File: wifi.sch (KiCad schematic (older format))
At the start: 1 part

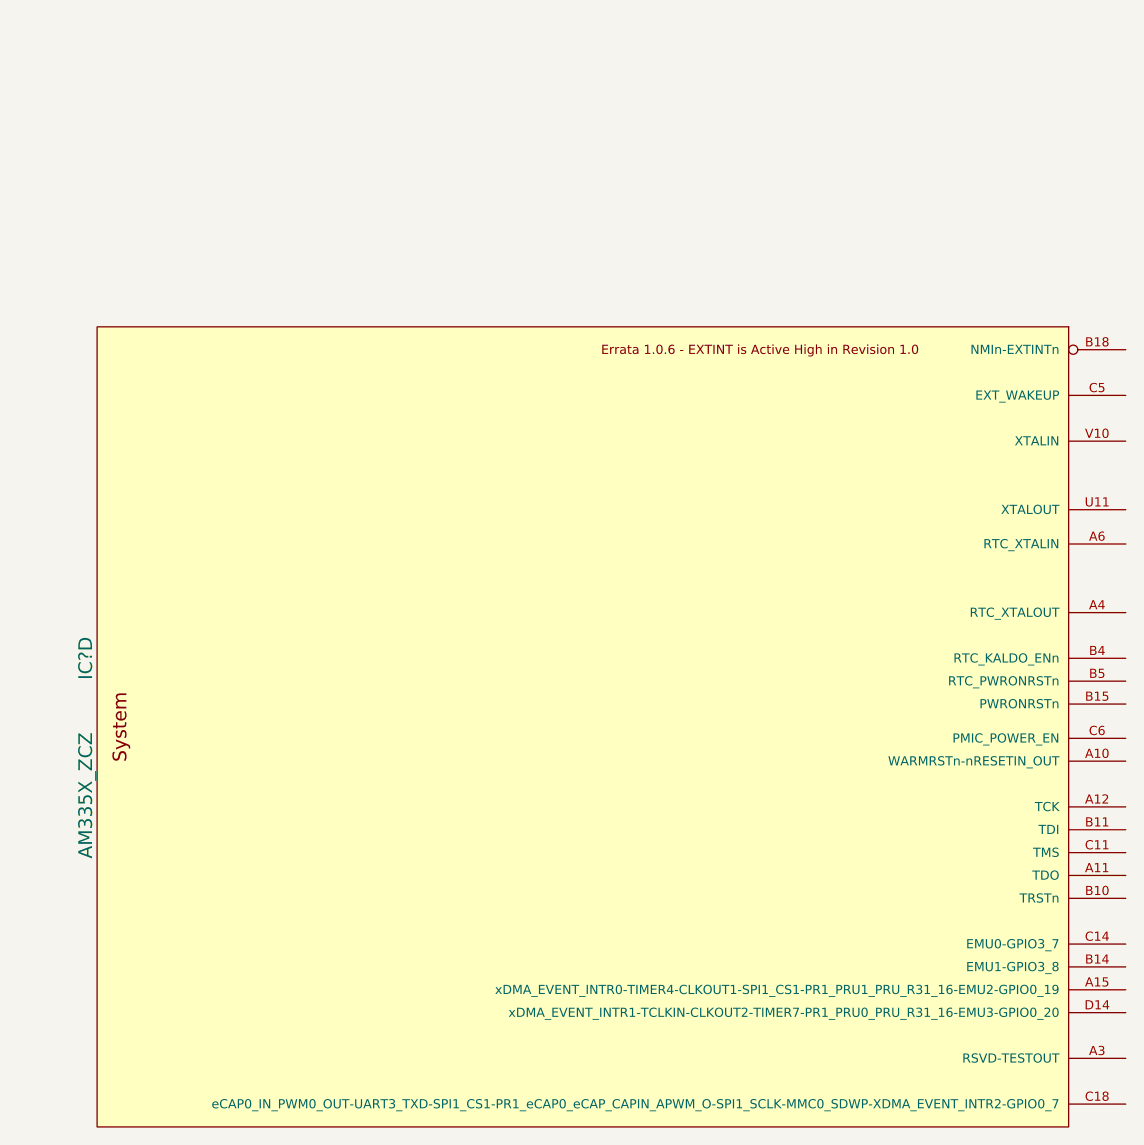
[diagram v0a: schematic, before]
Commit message: hierarchical sheets defined
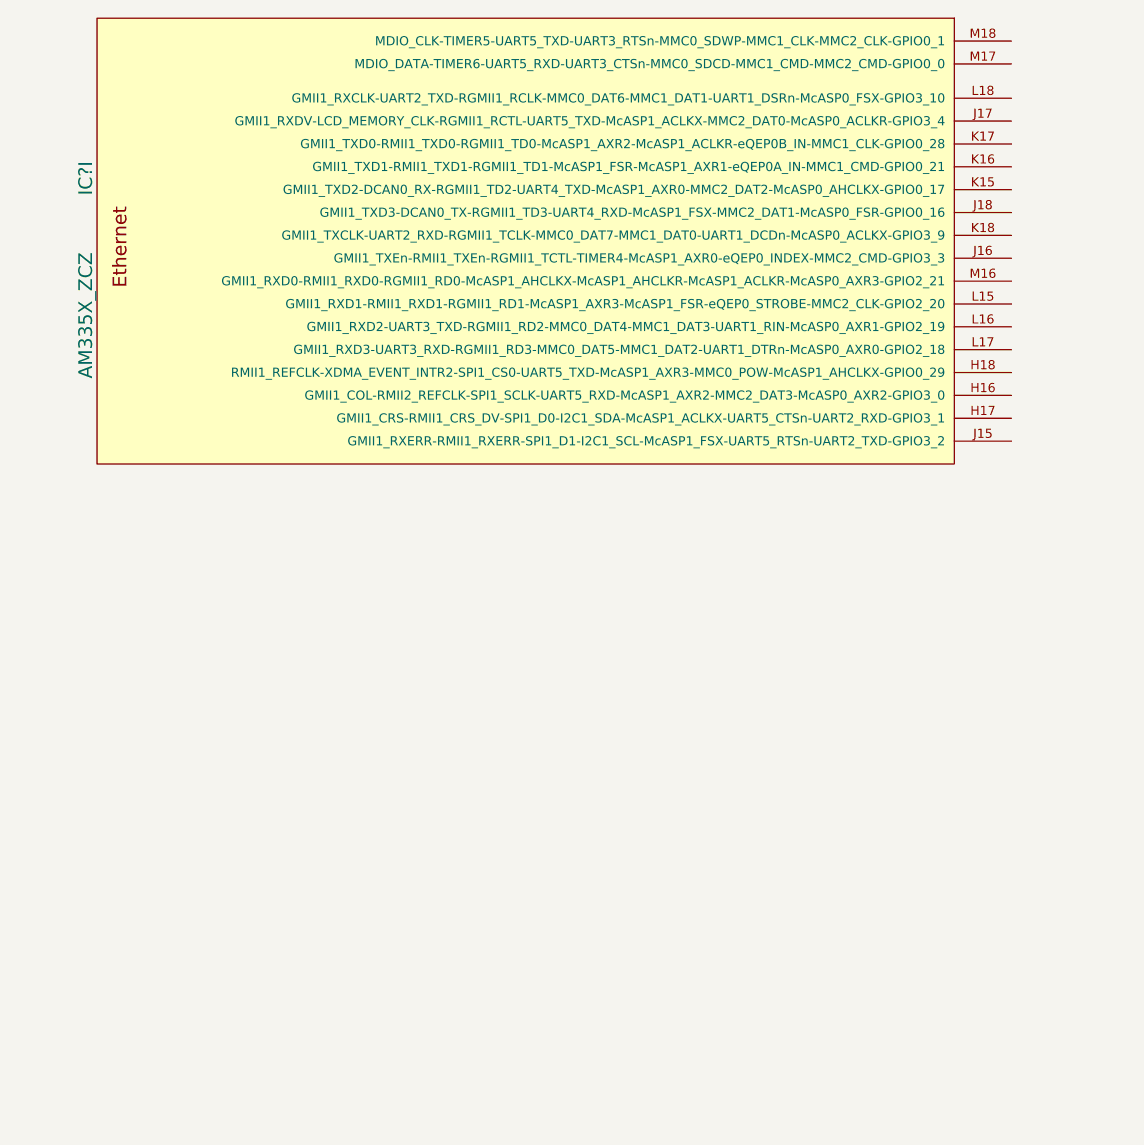
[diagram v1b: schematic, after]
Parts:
- removed IC?: AM335X_ZCZ, symbol AM335X_ZCZ
- added IC?: AM335X_ZCZ, symbol AM335X_ZCZ
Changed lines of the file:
@@
 $Descr A4 11693 8268
 encoding utf-8
-Sheet 6 9
+Sheet 9 9
 Title ""
 Date ""
@@
 $Comp
 L AM335X_ZCZ IC?
-U 4 1 58AC1D57
-P 725 3800
-AR Path="/58AC1D57" Ref="IC?"  Part="4"
-AR Path="/58AC1B74/58AC1D57" Ref="IC?"  Part="4"
-F 0 "IC?" V 675 4100 60  0000 C CNN
-F 1 "AM335X_ZCZ" V 675 3500 60  0000 C CNN
-F 2 "" H 725 3800 60  0001 C CNN
-F 3 "" H 725 3800 60  0001 C CNN
-	4    725  3800
+U 9 1 58AD666B
+P 725 1700
+F 0 "IC?" V 675 2000 60  0000 C CNN
+F 1 "AM335X_ZCZ" V 675 1400 60  0000 C CNN
+F 2 "" H 725 1700 60  0001 C CNN
+F 3 "" H 725 1700 60  0001 C CNN
+	9    725  1700
 	1    0    0    -1
 $EndComp

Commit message: wip wifi
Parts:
- added C? (x2): 100nF/6.3V, symbol C
- added R? (x7): 33, symbol R
- added R?: 1.5k, symbol R
- added R? (x6): 10k, symbol R
- added U?: TXS0108, symbol TXB0108
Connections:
- net WL_SDIO_D3.CPU: now reaches IC?.H16 (GMII1_COL-RMII2_REFCLK-SPI1_SCLK-UART5_RXD-McASP1_AXR2-MMC2_DAT3-McASP0_AXR2-GPIO3_0)
- net WL_SDIO_D3.CPU: now also R?.1
- net WL_IRQ.CPU: now reaches IC?.H18 (RMII1_REFCLK-XDMA_EVENT_INTR2-SPI1_CS0-UART5_TXD-McASP1_AXR3-MMC0_POW-McASP1_AHCLKX-GPIO0_29)
- net WL_SDIO_CMD.CPU: now reaches IC?.J16 (GMII1_TXEn-RMII1_TXEn-RGMII1_TCTL-TIMER4-McASP1_AXR0-eQEP0_INDEX-MMC2_CMD-GPIO3_3)
- net WL_SDIO_CMD.CPU: now also R?.1
- net WL_SDIO_D0.CPU: now reaches IC?.J17 (GMII1_RXDV-LCD_MEMORY_CLK-RGMII1_RCTL-UART5_TXD-McASP1_ACLKX-MMC2_DAT0-McASP0_ACLKR-GPIO3_4)
- net WL_SDIO_D0.CPU: now also R?.1
- net WL_SDIO_D1.CPU: now reaches IC?.J18 (GMII1_TXD3-DCAN0_TX-RGMII1_TD3-UART4_RXD-McASP1_FSX-MMC2_DAT1-McASP0_FSR-GPIO0_16)
- net WL_SDIO_D1.CPU: now also R?.1
- net WL_SDIO_D2.CPU: now reaches IC?.K15 (GMII1_TXD2-DCAN0_RX-RGMII1_TD2-UART4_TXD-McASP1_AXR0-MMC2_DAT2-McASP0_AHCLKX-GPIO0_17)
- net WL_SDIO_D2.CPU: now also R?.1
- net BT_EN.CPU: now reaches IC?.K17 (GMII1_TXD0-RMII1_TXD0-RGMII1_TD0-McASP1_AXR2-McASP1_ACLKR-eQEP0B_IN-MMC1_CLK-GPIO0_28)
- net WL_EN.CPU: now reaches IC?.K18 (GMII1_TXCLK-UART2_RXD-RGMII1_TCLK-MMC0_DAT7-MMC1_DAT0-UART1_DCDn-McASP0_ACLKX-GPIO3_9)
- net WL_SDIO_CLK.CPU: now reaches IC?.L15 (GMII1_RXD1-RMII1_RXD1-RGMII1_RD1-McASP1_AXR3-McASP1_FSR-eQEP0_STROBE-MMC2_CLK-GPIO2_20)
- net WL_SDIO_CLK.CPU: now also R?.1
- net BT_HCI_TX.CPU: now reaches IC?.L16 (GMII1_RXD2-UART3_TXD-RGMII1_RD2-MMC0_DAT4-MMC1_DAT3-UART1_RIN-McASP0_AXR1-GPIO2_19)
- net BT_HCI_RX.CPU: now reaches IC?.L17 (GMII1_RXD3-UART3_RXD-RGMII1_RD3-MMC0_DAT5-MMC1_DAT2-UART1_DTRn-McASP0_AXR0-GPIO2_18)
- net LS_BUF_OE.CPU: now reaches IC?.L18 (GMII1_RXCLK-UART2_TXD-RGMII1_RCLK-MMC0_DAT6-MMC1_DAT1-UART1_DSRn-McASP0_FSX-GPIO3_10)
- net LS_BUF_OE.CPU: now also R?.2
- net BT_HCI_CTS.CPU: now reaches IC?.M17 (MDIO_DATA-TIMER6-UART5_RXD-UART3_CTSn-MMC0_SDCD-MMC1_CMD-MMC2_CMD-GPIO0_0)
- net BT_HCI_RTS.CPU: now reaches IC?.M18 (MDIO_CLK-TIMER5-UART5_TXD-UART3_RTSn-MMC0_SDWP-MMC1_CLK-MMC2_CLK-GPIO0_1)
- new net: R?.2, U?.14 (B6)
- new net: R?.2, U?.15 (B5)
- new net: R?.2, U?.16 (B4)
- new net: R?.2, U?.17 (B3)
- new net: R?.2, U?.18 (B2)
- new net: R?.2, U?.20 (B1)
- new net GNDD: C?.1, C?.1, R?.1, U?.11 (GND)
- new net LS_BUF_OE: R?.1, R?.2, U?.10 (^OE)
- new net VDD_1V8_WIFI: C?.2, R?.1, R?.1, R?.1, R?.1, R?.1, R?.1, U?.2 (VccA)
- new net VDD_3V3_WIFI: C?.2, U?.19 (VccB)
- new net WL_SDIO_CLK: R?.2, U?.6 (A5)
- new net WL_SDIO_CMD: R?.2, U?.7 (A6)
- new net WL_SDIO_D0: R?.2, U?.1 (A1)
- new net WL_SDIO_D1: R?.2, U?.3 (A2)
- new net WL_SDIO_D2: R?.2, U?.4 (A3)
- new net WL_SDIO_D3: R?.2, U?.5 (A4)
- no-connect marks 0 -> 8

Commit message: wip wl1835 lib
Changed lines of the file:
@@
 EESchema Schematic File Version 2
+LIBS:mateboard-rescue
 LIBS:power
 LIBS:device
@@
 $EndComp
 Wire Wire Line
-	2950 3825 2950 3875
-Wire Wire Line
-	2950 3875 2950 3925
+	2950 3825 2950 3925
 Wire Wire Line
 	2950 3925 3000 3925
@@
 $EndComp
 Wire Wire Line
-	4300 3825 4300 3875
-Wire Wire Line
-	4300 3875 4300 3925
+	4300 3825 4300 3925
 Wire Wire Line
 	4300 3925 4200 3925
@@
 	1200 4825 2025 4825
 Wire Wire Line
-	2325 4825 2425 4825
-Wire Wire Line
-	2425 4825 3000 4825
+	2325 4825 3000 4825
 Wire Wire Line
 	2425 4875 2425 4825
@@
 	1100 4525 3000 4525
 Wire Wire Line
-	1100 3425 1100 3475
-Wire Wire Line
-	1100 3475 1100 3625
-Wire Wire Line
-	1100 3475 1225 3475
-Wire Wire Line
-	1225 3475 1350 3475
-Wire Wire Line
-	1350 3475 1475 3475
-Wire Wire Line
-	1475 3475 1600 3475
-Wire Wire Line
-	1600 3475 1725 3475
+	1100 3425 1100 3625
+Wire Wire Line
+	1100 3475 1725 3475
 Wire Wire Line
 	1725 3475 1725 3625

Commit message: wifi bt done
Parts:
- added AE?: ACA-5036-A2-CC-S, symbol Antenna_Shield
- added C? (x4): 100nF/6.3V, symbol C
- added C? (x3): 10pF, symbol C
- added C?: 1uF/6.3V, symbol C
- added C?: DNP 47uF, symbol CP
- added C?: 10uF/6.3V, symbol C
- added IC?: WL1835MODGBMOCT, symbol WL1835MODGBMOCT
- added J? (x2): ANT2, symbol CONN_COAXIAL
- added J? (x9): TEST_1P, symbol TEST_1P
- added R? (x14): 33, symbol R
- added R? (x2): 150k, symbol R
- added R? (x2): DNP 1k, symbol R
- added R?: DNP 10k, symbol R
- added R?: 1k, symbol R
- added R?: DNP 0R, symbol R
- added U?: TXS0108, symbol TXB0108
- added X?: NZ2520SB-32.768KHZ-NSA3534C, symbol OSCILLATOR
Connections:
- net BT_EN.CPU: now also R?.2
- net BT_HCI_CTS.CPU: now also R?.2, U?.15 (B5)
- net BT_HCI_RTS.CPU: now also R?.2, U?.13 (B7)
- net BT_HCI_RX.CPU: now also U?.14 (B6)
- net BT_HCI_TX.CPU: now also U?.20 (B1)
- net GNDD: now also AE?.2 (Shield), C?.1, C?.1, C?.1, C?.2, C?.2, C?.2, C?.2, IC?.1 (GND), IC?.15 (GND), IC?.16 (GND), IC?.17 (GND), IC?.19 (GND), IC?.20 (GND), IC?.23 (GND), IC?.24 (GND), IC?.28 (GND), IC?.29 (GND), IC?.30 (GND), IC?.31 (GND), IC?.33 (GND), IC?.34 (GND), IC?.35 (GND), IC?.37 (GND), IC?.39 (GND), IC?.44 (GND), IC?.45 (GND), IC?.48 (GND), IC?.49 (GND), IC?.54 (GND), IC?.55 (GND), IC?.59 (GND), IC?.61 (GND), IC?.63 (GND), IC?.64 (GND), IC?.7 (GND), IC?.9 (GND), IC?.PAD (G1-G36), J?.2 (Ext), J?.2 (Ext), R?.1, R?.1, R?.1, R?.1, U?.11 (GND), X?.2 (GND)
- net LS_BUF_OE: now also U?.10 (^OE)
- net VDD_1V8_WIFI: now also C?.1, C?.1, C?.2, C?.2, IC?.38 (VIO), R?.1, R?.1, U?.2 (VccA), X?.4 (VDD)
- net VDD_3V3_WIFI: now also C?.1, C?.1, C?.2, IC?.46 (VBAT_IN), IC?.47 (VBAT_IN), U?.19 (VccB)
- net WL_EN.CPU: now also R?.2
- net WL_IRQ.CPU: now also R?.2
- net WL_SDIO_CLK: now also R?.2
- net WL_SDIO_CMD: now also R?.2
- net WL_SDIO_D0: now also R?.2
- net WL_SDIO_D1: now also R?.2
- net WL_SDIO_D2: now also R?.2
- net WL_SDIO_D3: now also R?.2
- new net: IC?.10 (WL_SDIO_D0), R?.1
- new net: IC?.11 (WL_SDIO_D1), R?.1
- new net: IC?.12 (WL_SDIO_D2), R?.1
- new net: IC?.13 (WL_SDIO_D3), R?.1
- new net: IC?.14 (WLAN_IRQ), R?.1, R?.2
- new net: C?.1, IC?.18 (RF_ANT2)
- new net: IC?.25 (GPIO4), J?.1
- new net: IC?.26 (GPIO2), J?.1
- new net: IC?.27 (GPIO1), J?.1
- new net: C?.1, C?.2, IC?.32 (RF_ANT1)
- new net: IC?.42 (WL_UART_DBG), J?.1
- new net: IC?.43 (BT_UART_DBG), J?.1
- new net: IC?.50 (BT_HCI_RTS), R?.2
- new net: IC?.51 (BT_HCI_CTS), R?.2
- new net: IC?.52 (BT_HCI_TX), R?.2
- new net: IC?.53 (BT_HCI_RX), R?.2
- new net: IC?.56 (BT_AUD_IN), J?.1
- new net: IC?.57 (BT_AUD_OUT), J?.1
- new net: IC?.58 (BT_AUD_FSYNC), J?.1
- new net: IC?.6 (WL_SDIO_CMD), R?.1
- new net: IC?.60 (BT_AUD_CLK), J?.1
- new net: IC?.8 (WL_SDIO_CLK), R?.1
- new net: R?.1, U?.12 (B8)
- new net: R?.1, U?.17 (B3)
- new net: R?.1, U?.18 (B2)
- new net: C?.2, J?.1 (In) (x2)
- new net: AE?.1 (A), C?.1
- new net: R?.2, X?.1 (EN)
- new net 32.768kHz: IC?.36 (EXT_32K), R?.2, X?.3 (OUT)
- new net BT_EN: IC?.41 (BT_EN), R?.2, U?.4 (A3)
- new net BT_HCI_CTS: R?.1, U?.8 (A7)
- new net BT_HCI_RTS: R?.1, U?.6 (A5)
- new net BT_HCI_RX: R?.1, U?.1 (A1)
- new net BT_HCI_TX: R?.1, U?.7 (A6)
- new net CLKOUT2: U?.16 (B4)
- new net SLOW_CLK: R?.1, U?.5 (A4)
- new net WL_EN: IC?.40 (WLAN_EN), R?.2, U?.3 (A2)
- new net WL_IRQ: R?.2, U?.9 (A8)
- no-connect marks 8 -> 12
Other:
- note added: "Required to put\ndevice in debug\nmode."

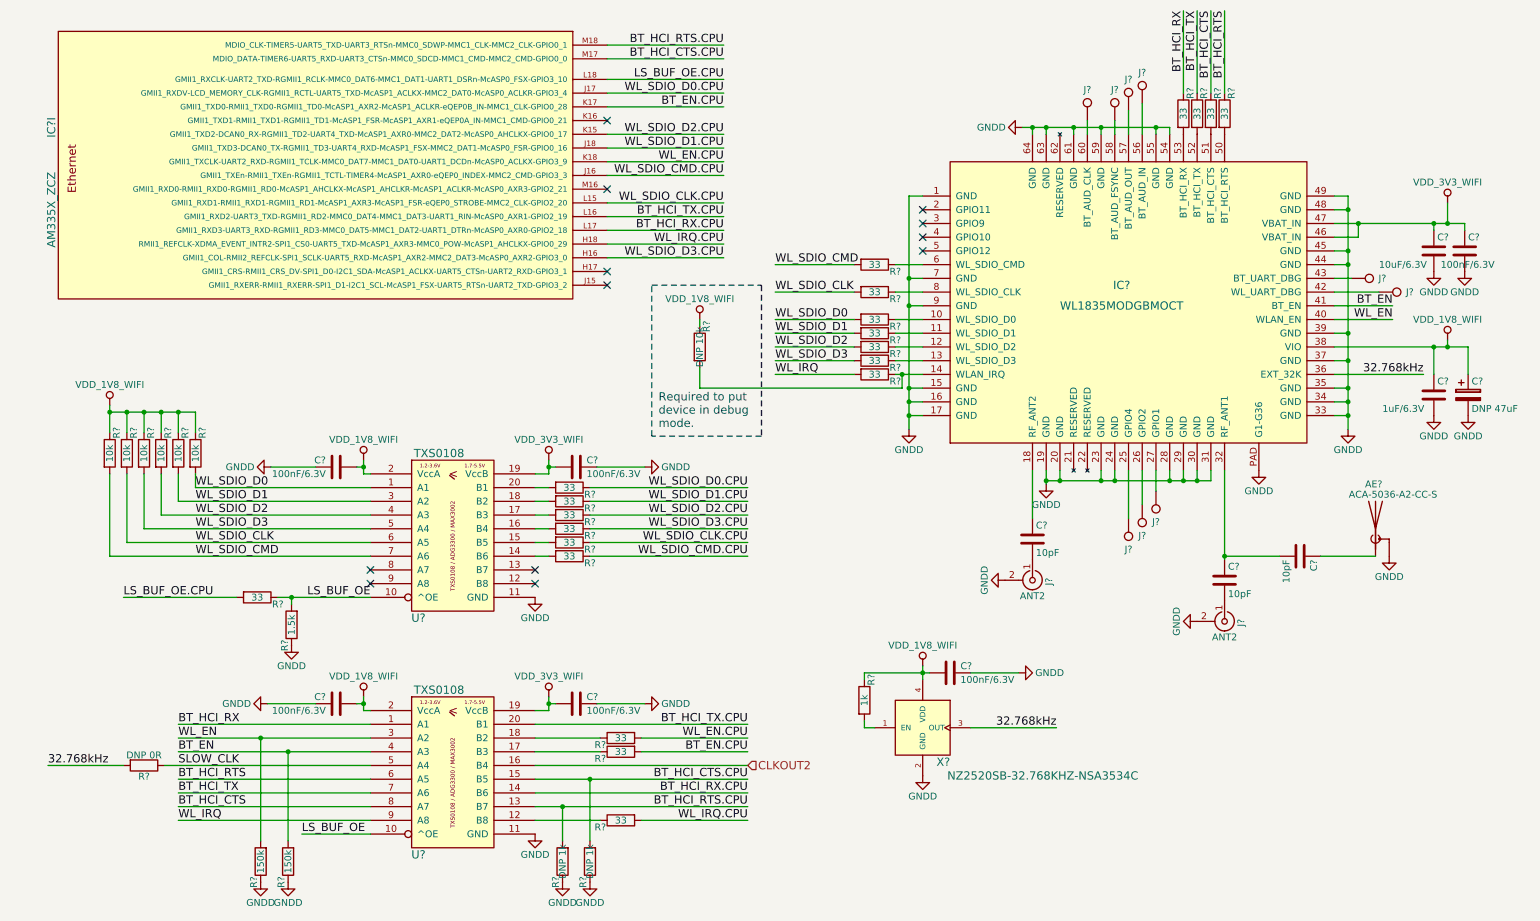
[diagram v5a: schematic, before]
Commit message: wifi bt leds
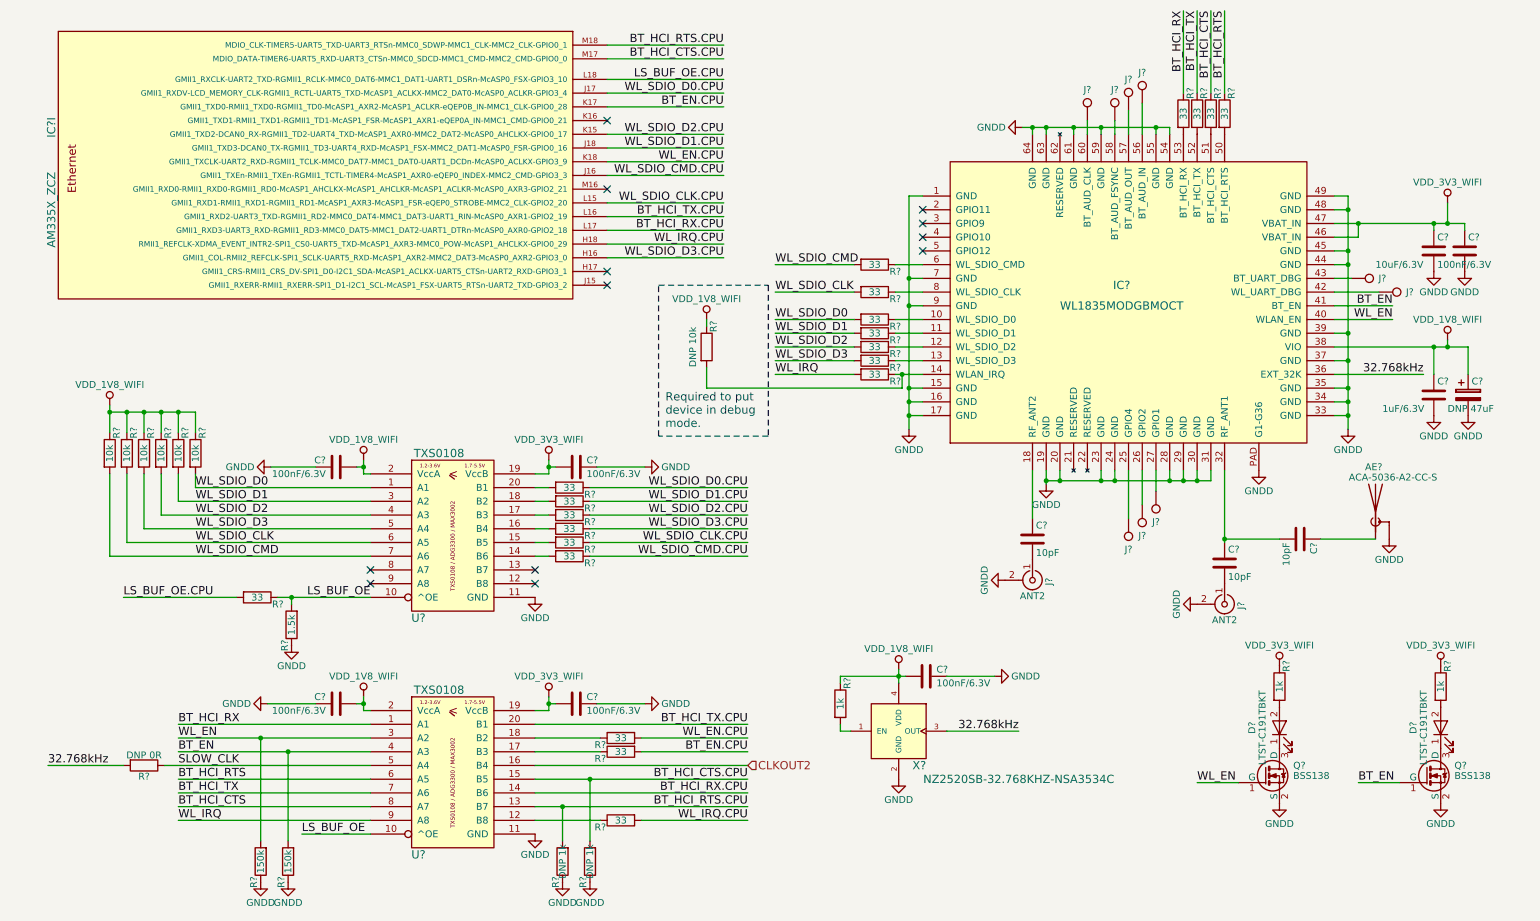
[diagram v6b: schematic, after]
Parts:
- added D? (x2): LTST-C191TBKT, symbol LED
- added Q? (x2): BSS138, TO_SOT_Packages_SMD:SOT-23, symbol BSS138
- added R? (x2): 1k, symbol R
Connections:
- net BT_EN: now also Q?.1 (G)
- net GNDD: now also Q?.2 (S), Q?.2 (S)
- net VDD_3V3_WIFI: now also R?.1, R?.1
- net WL_EN: now also Q?.1 (G)
- new net: D?.1 (K), Q?.3 (D) (x2)
- new net: D?.2 (A), R?.2 (x2)
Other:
- moved on the sheet: AE?, C?, J?, R?, X?
